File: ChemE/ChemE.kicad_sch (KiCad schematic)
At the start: 11 parts, among them IC1 LF353P, J1 Circuit Battery, J2 Car battery, J3 Motor, Q1 MTP3055E, U1 LM393N

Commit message: finished pcb
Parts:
- D1: footprint (none) -> OptoDevice:Osram_BPW82
- IC1: footprint DIP794W53P254L959H508Q8N -> op amp:DIP794W53P254L959H508Q8N
- J1: footprint (none) -> Connector_PinHeader_2.54mm:PinHeader_1x02_P2.54mm_Vertical
- Q1: footprint (none) -> Package_TO_SOT_THT:TO-247-3_Vertical
- R1, R2, R3: footprint (none) -> Resistor_SMD:R_1206_3216Metric_Pad1.30x1.75mm_HandSolder
- RV1: footprint (none) -> Potentiometer_THT:Potentiometer_ACP_CA9-H5_Horizontal
- U1: footprint LM393N:DIP794W45P254L959H508Q8 -> comparator:DIP794W45P254L959H508Q8
- batt_car1: renamed from J2; value Car battery -> Motor battery; footprint (none) -> Connector_PinHeader_2.54mm:PinHeader_1x02_P2.54mm_Vertical
- motor1: renamed from J3; footprint (none) -> Connector_PinHeader_2.54mm:PinHeader_1x02_P2.54mm_Vertical
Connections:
- net GND: now also batt_car1.2 (Pin_2); no longer motor1.2 (Pin_2)
- net at Q1.1 (D): now also motor1.2 (Pin_2); no longer batt_car1.2 (Pin_2)
- no-connect marks 0 -> 6
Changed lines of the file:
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@@
 		(color 0 0 0 0)
 	)
+	(no_connect
+		(at 137.16 72.39)
+	)
+	(no_connect
+		(at 137.16 67.31)
+	)
+	(no_connect
+		(at 209.55 67.31)
+	)
+	(no_connect
+		(at 173.99 67.31)
+	)
+	(no_connect
+		(at 173.99 72.39)
+	)
+	(no_connect
+		(at 137.16 69.85)
+	)
 	(wire
 		(pts
@@
 	(wire
 		(pts
+			(xy 231.14 30.48) (xy 231.14 34.29)
+		)
+		(stroke
+			(width 0)
+			(type default)
+		)
+	)
+	(wire
+		(pts
 			(xy 209.55 80.01) (xy 209.55 85.09)
 		)
@@
 	(wire
 		(pts
-			(xy 255.27 55.88) (xy 231.14 55.88)
-		)
-		(stroke
-			(width 0)
-			(type default)
-		)
-	)
-	(wire
-		(pts
 			(xy 148.59 69.85) (xy 173.99 69.85)
 		)
@@
 	(wire
 		(pts
-			(xy 231.14 55.88) (xy 231.14 30.48)
-		)
-		(stroke
-			(width 0)
-			(type default)
-		)
-	)
-	(wire
-		(pts
 			(xy 105.41 69.85) (xy 105.41 72.39)
 		)
@@
 	(wire
 		(pts
-			(xy 261.62 31.75) (xy 261.62 36.83)
-		)
-		(stroke
-			(width 0)
-			(type default)
-		)
-	)
-	(wire
-		(pts
 			(xy 109.22 69.85) (xy 105.41 69.85)
 		)
@@
 	(wire
 		(pts
-			(xy 255.27 72.39) (xy 255.27 77.47)
+			(xy 255.27 72.39) (xy 255.27 82.55)
 		)
 		(stroke
@@
 	(wire
 		(pts
+			(xy 261.62 31.75) (xy 261.62 55.88)
+		)
+		(stroke
+			(width 0)
+			(type default)
+		)
+	)
+	(wire
+		(pts
 			(xy 241.3 64.77) (xy 247.65 64.77)
 		)
@@
 	(wire
 		(pts
+			(xy 261.62 55.88) (xy 255.27 55.88)
+		)
+		(stroke
+			(width 0)
+			(type default)
+		)
+	)
+	(wire
+		(pts
 			(xy 220.98 30.48) (xy 224.79 30.48)
 		)
@@
 			(width 0)
 			(type default)
-		)
-	)
-	(label "M+"
-		(at 259.08 34.29 180)
-		(effects
-			(font
-				(size 1.27 1.27)
-			)
-			(justify right bottom)
-		)
-	)
-	(label "M-"
-		(at 255.27 77.47 0)
-		(effects
-			(font
-				(size 1.27 1.27)
-			)
-			(justify left bottom)
-		)
-	)
-	(label "M-"
-		(at 261.62 34.29 0)
-		(effects
-			(font
-				(size 1.27 1.27)
-			)
-			(justify left bottom)
 		)
 	)
@@
 	)
 	(symbol
-		(lib_id "power:GND")
-		(at 261.62 36.83 0)
-		(unit 1)
-		(exclude_from_sim no)
-		(in_bom yes)
-		(on_board yes)
-		(dnp no)
-		(fields_autoplaced yes)
-		(property "Reference" "#PWR010"
-			(at 261.62 43.18 0)
-			(effects
-				(font
-					(size 1.27 1.27)
-				)
-				(hide yes)
-			)
-		)
-		(property "Value" "GND"
-			(at 261.62 41.91 0)
-			(effects
-				(font
-					(size 1.27 1.27)
-				)
-			)
-		)
-		(property "Footprint" ""
-			(at 261.62 36.83 0)
-			(effects
-				(font
-					(size 1.27 1.27)
-				)
-				(hide yes)
-			)
-		)
-		(property "Datasheet" ""
-			(at 261.62 36.83 0)
-			(effects
-				(font
-					(size 1.27 1.27)
-				)
-				(hide yes)
-			)
-		)
-		(property "Description" "Power symbol creates a global label with name \"GND\" , ground"
-			(at 261.62 36.83 0)
-			(effects
-				(font
-					(size 1.27 1.27)
-				)
-				(hide yes)
-			)
-		)
-		(pin "1"
-		)
-		(instances
-			(project "ChemE"
-				(path "/39594484-eaea-4ff9-9430-fc8d8cc01f91"
-					(reference "#PWR010")
-					(unit 1)
-				)
-			)
-		)
-	)
-	(symbol
 		(lib_id "power:+9V")
 		(at 220.98 30.48 0)
@@
 			)
 		)
-		(property "Footprint" ""
+		(property "Footprint" "Resistor_SMD:R_1206_3216Metric_Pad1.30x1.75mm_HandSolder"
 			(at 243.078 68.58 90)
 			(effects
@@
 			)
 		)
-		(property "Footprint" ""
+		(property "Footprint" "Resistor_SMD:R_1206_3216Metric_Pad1.30x1.75mm_HandSolder"
 			(at 100.838 63.5 90)
 			(effects
@@
 			)
 		)
-		(property "Footprint" "LM393N:DIP794W45P254L959H508Q8"
+		(property "Footprint" "comparator:DIP794W45P254L959H508Q8"
 			(at 191.77 69.85 0)
 			(effects
@@
 			)
 		)
-		(property "Footprint" ""
+		(property "Footprint" "Potentiometer_THT:Potentiometer_ACP_CA9-H5_Horizontal"
 			(at 165.1 41.91 0)
 			(effects
@@
 	)
 	(symbol
+		(lib_id "power:GND")
+		(at 231.14 34.29 0)
+		(unit 1)
+		(exclude_from_sim no)
+		(in_bom yes)
+		(on_board yes)
+		(dnp no)
+		(fields_autoplaced yes)
+		(property "Reference" "#PWR013"
+			(at 231.14 40.64 0)
+			(effects
+				(font
+					(size 1.27 1.27)
+				)
+				(hide yes)
+			)
+		)
+		(property "Value" "GND"
+			(at 231.14 39.37 0)
+			(effects
+				(font
+					(size 1.27 1.27)
+				)
+			)
+		)
+		(property "Footprint" ""
+			(at 231.14 34.29 0)
+			(effects
+				(font
+					(size 1.27 1.27)
+				)
+				(hide yes)
+			)
+		)
+		(property "Datasheet" ""
+			(at 231.14 34.29 0)
+			(effects
+				(font
+					(size 1.27 1.27)
+				)
+				(hide yes)
+			)
+		)
+		(property "Description" "Power symbol creates a global label with name \"GND\" , ground"
+			(at 231.14 34.29 0)
+			(effects
+				(font
+					(size 1.27 1.27)
+				)
+				(hide yes)
+			)
+		)
+		(pin "1"
+		)
+		(instances
+			(project "ChemE"
+				(path "/39594484-eaea-4ff9-9430-fc8d8cc01f91"
+					(reference "#PWR013")
+					(unit 1)
+				)
+			)
+		)
+	)
+	(symbol
 		(lib_id "power:+9V")
 		(at 137.16 60.96 0)
@@
 			)
 		)
-		(property "Footprint" ""
+		(property "Footprint" "Connector_PinHeader_2.54mm:PinHeader_1x02_P2.54mm_Vertical"
 			(at 88.9 22.86 0)
 			(effects
@@
 		(dnp no)
 		(fields_autoplaced yes)
-		(property "Reference" "J3"
+		(property "Reference" "motor1"
 			(at 262.89 26.0349 90)
 			(effects
@@
 			)
 		)
-		(property "Footprint" ""
+		(property "Footprint" "Connector_PinHeader_2.54mm:PinHeader_1x02_P2.54mm_Vertical"
 			(at 259.08 26.67 0)
 			(effects
@@
 			(project "ChemE"
 				(path "/39594484-eaea-4ff9-9430-fc8d8cc01f91"
-					(reference "J3")
+					(reference "motor1")
+					(unit 1)
+				)
+			)
+		)
+	)
+	(symbol
+		(lib_id "power:GND")
+		(at 255.27 82.55 0)
+		(unit 1)
+		(exclude_from_sim no)
+		(in_bom yes)
+		(on_board yes)
+		(dnp no)
+		(fields_autoplaced yes)
+		(property "Reference" "#PWR010"
+			(at 255.27 88.9 0)
+			(effects
+				(font
+					(size 1.27 1.27)
+				)
+				(hide yes)
+			)
+		)
+		(property "Value" "GND"
+			(at 255.27 87.63 0)
+			(effects
+				(font
+					(size 1.27 1.27)
+				)
+			)
+		)
+		(property "Footprint" ""
+			(at 255.27 82.55 0)
+			(effects
+				(font
+					(size 1.27 1.27)
+				)
+				(hide yes)
+			)
+		)
+		(property "Datasheet" ""
+			(at 255.27 82.55 0)
+			(effects
+				(font
+					(size 1.27 1.27)
+				)
+				(hide yes)
+			)
+		)
+		(property "Description" "Power symbol creates a global label with name \"GND\" , ground"
+			(at 255.27 82.55 0)
+			(effects
+				(font
+					(size 1.27 1.27)
+				)
+				(hide yes)
+			)
+		)
+		(pin "1"
+		)
+		(instances
+			(project "ChemE"
+				(path "/39594484-eaea-4ff9-9430-fc8d8cc01f91"
+					(reference "#PWR010")
 					(unit 1)
 				)
@@
 			)
 		)
-		(property "Footprint" ""
+		(property "Footprint" "OptoDevice:Osram_BPW82"
 			(at 80.01 71.12 0)
 			(effects
@@
 			)
 		)
-		(property "Footprint" ""
+		(property "Footprint" "Resistor_SMD:R_1206_3216Metric_Pad1.30x1.75mm_HandSolder"
 			(at 232.41 66.548 90)
 			(effects
@@
 			)
 		)
-		(property "Footprint" ""
+		(property "Footprint" "Package_TO_SOT_THT:TO-247-3_Vertical"
 			(at 257.81 62.23 0)
 			(effects
@@
 			)
 		)
-		(property "Footprint" "DIP794W53P254L959H508Q8N"
+		(property "Footprint" "op amp:DIP794W53P254L959H508Q8N"
 			(at 133.35 159.69 0)
 			(effects
@@
 		(dnp no)
 		(fields_autoplaced yes)
-		(property "Reference" "J2"
+		(property "Reference" "batt_car1"
 			(at 228.6 24.7649 90)
 			(effects
@@
 			)
 		)
-		(property "Value" "Car battery"
+		(property "Value" "Motor battery"
 			(at 228.6 27.3049 90)
 			(effects
@@
 			)
 		)
-		(property "Footprint" ""
+		(property "Footprint" "Connector_PinHeader_2.54mm:PinHeader_1x02_P2.54mm_Vertical"
 			(at 224.79 25.4 0)
 			(effects
@@
 			(project "ChemE"
 				(path "/39594484-eaea-4ff9-9430-fc8d8cc01f91"
-					(reference "J2")
-					(unit 1)
-				)
+					(reference "batt_car1")
+					(unit 1)
+				)

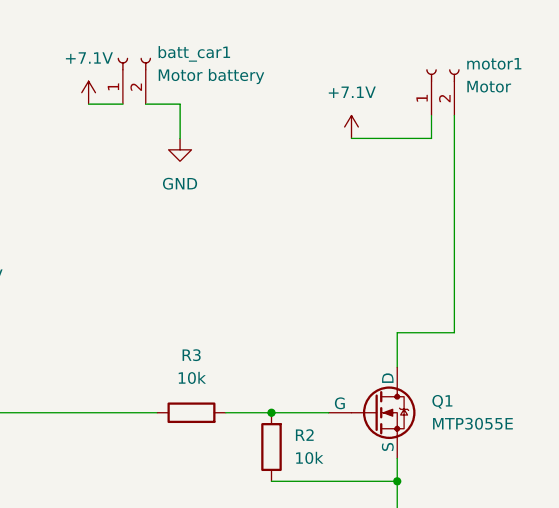
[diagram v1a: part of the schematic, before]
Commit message: updated sch to have all tht. added 1n004
pcb has not been updated yet. last push has last sch and pcb with the smd resistors.
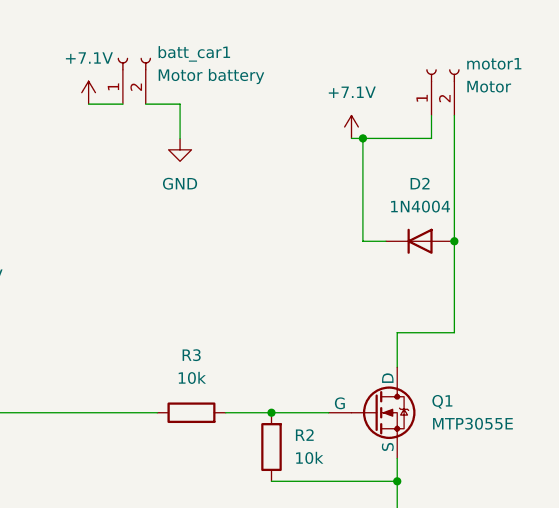
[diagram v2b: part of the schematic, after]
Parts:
- added D2: 1N4004, Diode_THT:D_DO-41_SOD81_P10.16mm_Horizontal, symbol Diode:1N4004
- R1, R2, R3: footprint Resistor_SMD:R_1206_3216Metric_Pad1.30x1.75mm_HandSolder -> Resistor_THT:R_Axial_DIN0204_L3.6mm_D1.6mm_P2.54mm_Vertical
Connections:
- net +7.1V: now also D2.1 (K)
- net at Q1.1 (D), motor1.2 (Pin_2): now also D2.2 (A)
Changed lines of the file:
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@@
 	(paper "A4")
+	(junction
+		(at 251.46 34.29)
+		(diameter 0)
+		(color 0 0 0 0)
+	)
 	(junction
 		(at 255.27 72.39)
@@
 	)
 	(junction
+		(at 261.62 45.72)
+		(diameter 0)
+		(color 0 0 0 0)
+	)
+	(junction
 		(at 99.06 59.69)
 		(diameter 0)
@@
 	(wire
 		(pts
-			(xy 250.19 34.29) (xy 259.08 34.29)
+			(xy 250.19 34.29) (xy 251.46 34.29)
 		)
 		(stroke
@@
 	(wire
 		(pts
+			(xy 261.62 45.72) (xy 261.62 55.88)
+		)
+		(stroke
+			(width 0)
+			(type default)
+		)
+	)
+	(wire
+		(pts
 			(xy 255.27 72.39) (xy 255.27 82.55)
 		)
@@
 	(wire
 		(pts
+			(xy 251.46 45.72) (xy 251.46 34.29)
+		)
+		(stroke
+			(width 0)
+			(type default)
+		)
+	)
+	(wire
+		(pts
 			(xy 227.33 30.48) (xy 231.14 30.48)
 		)
@@
 	(wire
 		(pts
-			(xy 261.62 31.75) (xy 261.62 55.88)
+			(xy 261.62 31.75) (xy 261.62 45.72)
 		)
 		(stroke
@@
 	(wire
 		(pts
+			(xy 254 45.72) (xy 251.46 45.72)
+		)
+		(stroke
+			(width 0)
+			(type default)
+		)
+	)
+	(wire
+		(pts
 			(xy 255.27 59.69) (xy 255.27 55.88)
 		)
@@
 		(pts
 			(xy 255.27 69.85) (xy 255.27 72.39)
+		)
+		(stroke
+			(width 0)
+			(type default)
+		)
+	)
+	(wire
+		(pts
+			(xy 251.46 34.29) (xy 259.08 34.29)
 		)
 		(stroke
@@
 	)
 	(symbol
+		(lib_id "Diode:1N4004")
+		(at 257.81 45.72 0)
+		(unit 1)
+		(exclude_from_sim no)
+		(in_bom yes)
+		(on_board yes)
+		(dnp no)
+		(fields_autoplaced yes)
+		(property "Reference" "D2"
+			(at 257.81 39.37 0)
+			(effects
+				(font
+					(size 1.27 1.27)
+				)
+			)
+		)
+		(property "Value" "1N4004"
+			(at 257.81 41.91 0)
+			(effects
+				(font
+					(size 1.27 1.27)
+				)
+			)
+		)
+		(property "Footprint" "Diode_THT:D_DO-41_SOD81_P10.16mm_Horizontal"
+			(at 257.81 50.165 0)
+			(effects
+				(font
+					(size 1.27 1.27)
+				)
+				(hide yes)
+			)
+		)
+		(property "Datasheet" "http://www.vishay.com/docs/88503/1n4001.pdf"
+			(at 257.81 45.72 0)
+			(effects
+				(font
+					(size 1.27 1.27)
+				)
+				(hide yes)
+			)
+		)
+		(property "Description" "400V 1A General Purpose Rectifier Diode, DO-41"
+			(at 257.81 45.72 0)
+			(effects
+				(font
+					(size 1.27 1.27)
+				)
+				(hide yes)
+			)
+		)
+		(property "Sim.Device" "D"
+			(at 257.81 45.72 0)
+			(effects
+				(font
+					(size 1.27 1.27)
+				)
+				(hide yes)
+			)
+		)
+		(property "Sim.Pins" "1=K 2=A"
+			(at 257.81 45.72 0)
+			(effects
+				(font
+					(size 1.27 1.27)
+				)
+				(hide yes)
+			)
+		)
+		(pin "2"
+		)
+		(pin "1"
+		)
+		(instances
+			(project ""
+				(path "/39594484-eaea-4ff9-9430-fc8d8cc01f91"
+					(reference "D2")
+					(unit 1)
+				)
+			)
+		)
+	)
+	(symbol
 		(lib_id "power:+9V")
 		(at 250.19 34.29 0)
@@
 			)
 		)
-		(property "Footprint" "Resistor_SMD:R_1206_3216Metric_Pad1.30x1.75mm_HandSolder"
+		(property "Footprint" "Resistor_THT:R_Axial_DIN0204_L3.6mm_D1.6mm_P2.54mm_Vertical"
 			(at 243.078 68.58 90)
 			(effects
@@
 			)
 		)
-		(property "Footprint" "Resistor_SMD:R_1206_3216Metric_Pad1.30x1.75mm_HandSolder"
+		(property "Footprint" "Resistor_THT:R_Axial_DIN0204_L3.6mm_D1.6mm_P2.54mm_Vertical"
 			(at 100.838 63.5 90)
 			(effects
@@
 			)
 		)
-		(property "Footprint" "Resistor_SMD:R_1206_3216Metric_Pad1.30x1.75mm_HandSolder"
+		(property "Footprint" "Resistor_THT:R_Axial_DIN0204_L3.6mm_D1.6mm_P2.54mm_Vertical"
 			(at 232.41 66.548 90)
 			(effects

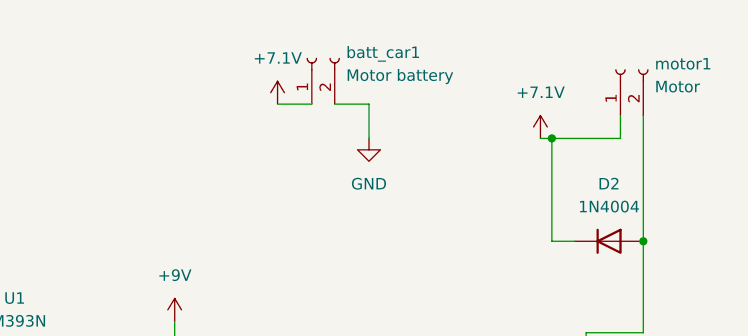
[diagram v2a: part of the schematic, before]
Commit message: increased trace width, made tht
increased trace width from .5mm to 1mm and made everything THT.
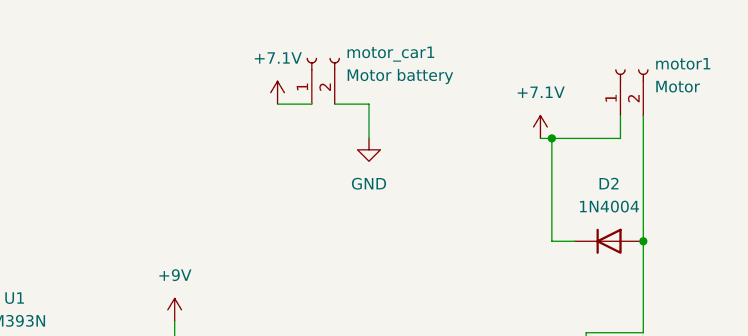
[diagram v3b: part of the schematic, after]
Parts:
- renumbered batt_car1 to motor_car1
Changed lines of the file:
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@@
 		(dnp no)
 		(fields_autoplaced yes)
-		(property "Reference" "batt_car1"
+		(property "Reference" "motor_car1"
 			(at 228.6 24.7649 90)
 			(effects
@@
 			(project "ChemE"
 				(path "/39594484-eaea-4ff9-9430-fc8d8cc01f91"
-					(reference "batt_car1")
+					(reference "motor_car1")
 					(unit 1)
 				)

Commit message: annoted the sch
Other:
- note added: "9V batt connector"
- note added: "DC motor connector"
- note added: "MOSFET"
- note added: "comparator. when we're changing (known from the TIA), it compares the TIA voltage (v_comp) to the reference (9v, v_ref) voltage If we're changing (so v_ref <= v_comp), a HIGH signal is sent. when this high signal is sent, the mosfet (a gate) OPENS and allows the power from the car battery to power the motor."
- note added: "motor battery connector"
- note added: "potentiometer for tuning"
- note added: "transimpedence amplifier (TIA) - converts the current to a voltage"
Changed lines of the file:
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@@
 	(generator_version "9.0")
 	(paper "A4")
+	(text "potentiometer for tuning"
+		(exclude_from_sim no)
+		(at 178.054 37.338 0)
+		(effects
+			(font
+				(size 1.27 1.27)
+			)
+		)
+	)
+	(text "transimpedence amplifier (TIA) - converts the current to a voltage"
+		(exclude_from_sim no)
+		(at 106.426 93.218 0)
+		(effects
+			(font
+				(size 1.27 1.27)
+			)
+		)
+	)
+	(text "motor battery connector"
+		(exclude_from_sim no)
+		(at 224.79 20.574 0)
+		(effects
+			(font
+				(size 1.27 1.27)
+			)
+		)
+	)
+	(text "DC motor connector"
+		(exclude_from_sim no)
+		(at 260.858 20.066 0)
+		(effects
+			(font
+				(size 1.27 1.27)
+			)
+		)
+	)
+	(text "MOSFET"
+		(exclude_from_sim no)
+		(at 262.382 60.706 0)
+		(effects
+			(font
+				(size 1.27 1.27)
+			)
+		)
+	)
+	(text "comparator. when we're changing (known from the TIA), it compares the TIA voltage (v_comp) to the \nreference (9v, v_ref) voltage\n\nIf we're changing (so v_ref <= v_comp), a HIGH signal is sent.\nwhen this high signal is sent, the mosfet (a gate) OPENS and allows the power from\nthe car battery to power the motor.\n"
+		(exclude_from_sim no)
+		(at 211.328 102.616 0)
+		(effects
+			(font
+				(size 1.27 1.27)
+			)
+		)
+	)
+	(text "9V batt connector"
+		(exclude_from_sim no)
+		(at 90.17 36.83 0)
+		(effects
+			(font
+				(size 1.27 1.27)
+			)
+		)
+	)
 	(junction
 		(at 251.46 34.29)
